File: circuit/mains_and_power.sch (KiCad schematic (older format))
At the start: 28 parts, among them J1 Screw_Terminal_01x10, U1 AQH3223, U2 AQH3223, U3 AQH3223, U4 MPM-05-12, U5 TC7660SEOA, U6 AP5100

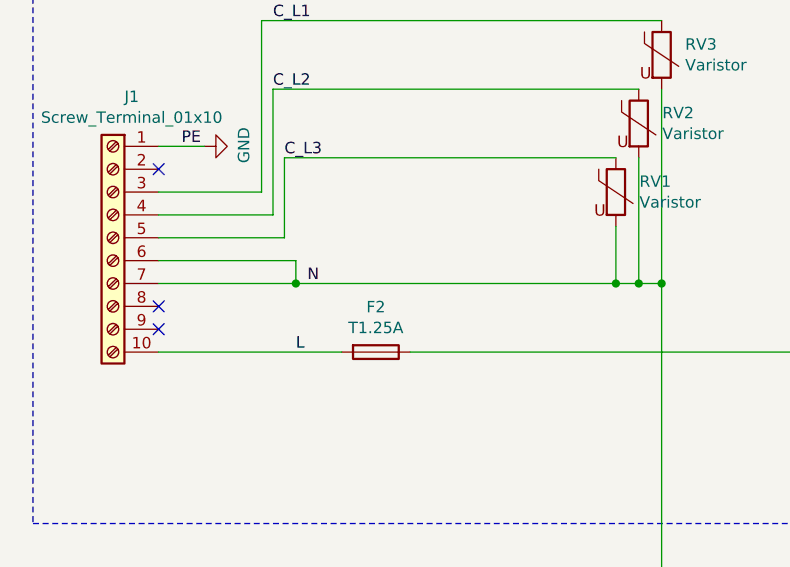
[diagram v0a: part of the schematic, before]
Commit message: Finish schematic rev1 and footprint assignment
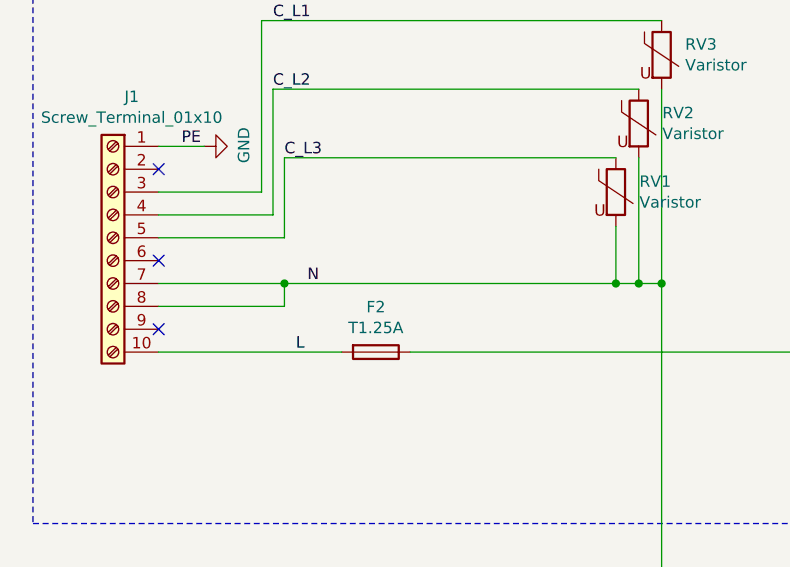
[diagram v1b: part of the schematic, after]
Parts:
- C1, C10, C11, C2, C3, C5, C6, C8: PartNo (none) -> 963-EMK212ABJ106MG-T
- C26: footprint (none) -> Capacitor_SMD:C_0805_2012Metric_Pad1.15x1.40mm_HandSolder; PartNo (none) -> 77-VJ0805Y101KXACBC
- C4, C7, C9: footprint Capacitor_SMD:C_0603_1608Metric_Pad1.05x0.95mm_HandSolder -> Capacitor_SMD:C_0805_2012Metric_Pad1.15x1.40mm_HandSolder; PartNo (none) -> 963-EMF212B7104KGHT
- J1: footprint (none) -> atmevse-footprints:CUI_TB005-762-10GR; PartNo 651-1707111 -> 490-TB005-762-10BE
- U1, U2, U3: PartNo (none) -> 769-AQH1213AX
- U4: footprint Converter_ACDC:Converter_ACDC_MeanWell_IRM-05-xx_THT -> Converter_ACDC:Converter_ACDC_MeanWell_IRM-10-xx_THT; PartNo (none) -> 709-IRM10-12
- U5: PartNo (none) -> 579-TC7660SEOA
- U6: PartNo (none) -> 621-AP5100WG-7
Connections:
- net N: now also J1.8 (Pin_8); no longer J1.6 (Pin_6)
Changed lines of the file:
@@
 Sheet 2 4
 Title ""
-Date "2020-05-29"
-Rev "0.7"
+Date "2020-06-01"
+Rev "1.0"
 Comp ""
 Comment1 "DONE: Replaced buck regulator AOZ1280 -> AP5100"
@@
 F 3 "" H 5200 3800 50  0001 C CNN
 F 4 "" H 5200 3800 50  0001 C CNN "Part"
-F 5 "" H 5200 3800 50  0001 C CNN "PartNo"
+F 5 "769-AQH1213AX" H 5200 3800 50  0001 C CNN "PartNo"
 F 6 "Mouser" H 5200 3800 50  0001 C CNN "Supplier"
 	1    5200 3800
@@
 F 3 "" H 5200 2800 50  0001 C CNN
 F 4 "" H 5200 2800 50  0001 C CNN "Part"
-F 5 "" H 5200 2800 50  0001 C CNN "PartNo"
+F 5 "769-AQH1213AX" H 5200 2800 50  0001 C CNN "PartNo"
 F 6 "Mouser" H 5200 2800 50  0001 C CNN "Supplier"
 	1    5200 2800
@@
 F 3 "" H 5200 1800 50  0001 C CNN
 F 4 "" H 5200 1800 50  0001 C CNN "Part"
-F 5 "" H 5200 1800 50  0001 C CNN "PartNo"
+F 5 "769-AQH1213AX" H 5200 1800 50  0001 C CNN "PartNo"
 F 6 "Mouser" H 5200 1800 50  0001 C CNN "Supplier"
 	1    5200 1800
@@
 F 0 "U4" H 5200 5447 42  0000 C CNN
 F 1 "MPM-05-12" H 5200 5368 42  0000 C CNN
-F 2 "Converter_ACDC:Converter_ACDC_MeanWell_IRM-05-xx_THT" H 5200 5000 50  0001 C CNN
+F 2 "Converter_ACDC:Converter_ACDC_MeanWell_IRM-10-xx_THT" H 5200 5000 50  0001 C CNN
 F 3 "https://www.meanwell.com/webapp/product/search.aspx?prod=MPM-05" H 5200 5000 50  0001 C CNN
 F 4 "" H 5200 5000 50  0001 C CNN "Part"
-F 5 "" H 5200 5000 50  0001 C CNN "PartNo"
+F 5 "709-IRM10-12" H 5200 5000 50  0001 C CNN "PartNo"
 F 6 "Mouser" H 5200 5000 50  0001 C CNN "Supplier"
 	1    5200 5000
@@
 F 3 "~" H 6700 1850 50  0001 C CNN
 F 4 "" H 6700 1850 50  0001 C CNN "Part"
-F 5 "" H 6700 1850 50  0001 C CNN "PartNo"
+F 5 "963-EMK212ABJ106MG-T" H 6700 1850 50  0001 C CNN "PartNo"
 F 6 "Mouser" H 6700 1850 50  0001 C CNN "Supplier"
 	1    6700 1850
@@
 F 3 "~" H 7050 1850 50  0001 C CNN
 F 4 "" H 7050 1850 50  0001 C CNN "Part"
-F 5 "" H 7050 1850 50  0001 C CNN "PartNo"
+F 5 "963-EMK212ABJ106MG-T" H 7050 1850 50  0001 C CNN "PartNo"
 F 6 "Mouser" H 7050 1850 50  0001 C CNN "Supplier"
 	1    7050 1850
@@
 F 3 "~" H 7400 1850 50  0001 C CNN
 F 4 "" H 7400 1850 50  0001 C CNN "Part"
-F 5 "" H 7400 1850 50  0001 C CNN "PartNo"
+F 5 "963-EMK212ABJ106MG-T" H 7400 1850 50  0001 C CNN "PartNo"
 F 6 "Mouser" H 7400 1850 50  0001 C CNN "Supplier"
 	1    7400 1850
@@
 F 3 "~" H 7750 1850 50  0001 C CNN
 F 4 "" H 7750 1850 50  0001 C CNN "Part"
-F 5 "" H 7750 1850 50  0001 C CNN "PartNo"
+F 5 "963-EMK212ABJ106MG-T" H 7750 1850 50  0001 C CNN "PartNo"
 F 6 "Mouser" H 7750 1850 50  0001 C CNN "Supplier"
 	1    7750 1850
@@
 F 0 "C7" H 8215 1896 50  0000 L CNN
 F 1 "100n" V 8250 1650 50  0000 L CNN
-F 2 "Capacitor_SMD:C_0603_1608Metric_Pad1.05x0.95mm_HandSolder" H 8138 1700 50  0001 C CNN
+F 2 "Capacitor_SMD:C_0805_2012Metric_Pad1.15x1.40mm_HandSolder" H 8138 1700 50  0001 C CNN
 F 3 "~" H 8100 1850 50  0001 C CNN
 F 4 "" H 8100 1850 50  0001 C CNN "Part"
-F 5 "" H 8100 1850 50  0001 C CNN "PartNo"
+F 5 "963-EMF212B7104KGHT " H 8100 1850 50  0001 C CNN "PartNo"
 F 6 "Mouser" H 8100 1850 50  0001 C CNN "Supplier"
 	1    8100 1850
@@
 F 0 "C9" V 9271 1550 50  0000 C CNN
 F 1 "100n" V 9362 1550 50  0000 C CNN
-F 2 "Capacitor_SMD:C_0603_1608Metric_Pad1.05x0.95mm_HandSolder" H 9500 1550 50  0001 C CNN
+F 2 "Capacitor_SMD:C_0805_2012Metric_Pad1.15x1.40mm_HandSolder" H 9500 1550 50  0001 C CNN
 F 3 "~" H 9500 1550 50  0001 C CNN
 F 4 "" H 9500 1550 50  0001 C CNN "Part"
-F 5 "" H 9500 1550 50  0001 C CNN "PartNo"
+F 5 "963-EMF212B7104KGHT " H 9500 1550 50  0001 C CNN "PartNo"
 F 6 "Mouser" H 9500 1550 50  0001 C CNN "Supplier"
 	1    9500 1550
@@
 F 3 "~" H 10700 1850 50  0001 C CNN
 F 4 "" H 10700 1850 50  0001 C CNN "Part"
-F 5 "" H 10700 1850 50  0001 C CNN "PartNo"
+F 5 "963-EMK212ABJ106MG-T" H 10700 1850 50  0001 C CNN "PartNo"
 F 6 "Mouser" H 10700 1850 50  0001 C CNN "Supplier"
 	1    10700 1850
@@
 F 3 "~" H 11000 1850 50  0001 C CNN
 F 4 "" H 11000 1850 50  0001 C CNN "Part"
-F 5 "" H 11000 1850 50  0001 C CNN "PartNo"
+F 5 "963-EMK212ABJ106MG-T" H 11000 1850 50  0001 C CNN "PartNo"
 F 6 "Mouser" H 11000 1850 50  0001 C CNN "Supplier"
 	1    11000 1850
@@
 F 3 "https://www.mouser.de/datasheet/2/268/21467B-1180369.pdf" H 8900 4350 50  0001 C CNN
 F 4 "" H 8900 4350 50  0001 C CNN "Part"
-F 5 "" H 8900 4350 50  0001 C CNN "PartNo"
+F 5 "579-TC7660SEOA" H 8900 4350 50  0001 C CNN "PartNo"
 F 6 "Mouser" H 8900 4350 50  0001 C CNN "Supplier"
 	1    8900 4350
@@
 F 0 "C4" H 7965 3996 50  0000 L CNN
 F 1 "100n" V 8000 3750 50  0000 L CNN
-F 2 "Capacitor_SMD:C_0603_1608Metric_Pad1.05x0.95mm_HandSolder" H 7888 3800 50  0001 C CNN
+F 2 "Capacitor_SMD:C_0805_2012Metric_Pad1.15x1.40mm_HandSolder" H 7888 3800 50  0001 C CNN
 F 3 "~" H 7850 3950 50  0001 C CNN
 F 4 "" H 7850 3950 50  0001 C CNN "Part"
-F 5 "" H 7850 3950 50  0001 C CNN "PartNo"
+F 5 "963-EMF212B7104KGHT " H 7850 3950 50  0001 C CNN "PartNo"
 F 6 "Mouser" H 7850 3950 50  0001 C CNN "Supplier"
 	1    7850 3950
@@
 F 3 "~" H 7500 4400 50  0001 C CNN
 F 4 "" H 7500 4400 50  0001 C CNN "Part"
-F 5 "" H 7500 4400 50  0001 C CNN "PartNo"
+F 5 "963-EMK212ABJ106MG-T" H 7500 4400 50  0001 C CNN "PartNo"
 F 6 "Mouser" H 7500 4400 50  0001 C CNN "Supplier"
 	1    7500 4400
@@
 F 3 "~" H 9700 4750 50  0001 C CNN
 F 4 "" H 9700 4750 50  0001 C CNN "Part"
-F 5 "" H 9700 4750 50  0001 C CNN "PartNo"
+F 5 "963-EMK212ABJ106MG-T" H 9700 4750 50  0001 C CNN "PartNo"
 F 6 "Mouser" H 9700 4750 50  0001 C CNN "Supplier"
 	1    9700 4750
@@
 F 0 "J1" H 818 3467 50  0000 C CNN
 F 1 "Screw_Terminal_01x10" H 818 3376 50  0000 C CNN
-F 2 "" H 900 2850 50  0001 C CNN
+F 2 "atmevse-footprints:CUI_TB005-762-10GR" H 900 2850 50  0001 C CNN
 F 3 "https://www.phoenixcontact.com/online/portal/us?uri=pxc-oc-itemdetail:pid=1707111&library=usen&pdfmode=direct&pdflanguage=en" H 900 2850 50  0001 C CNN
 F 4 "" H 900 2850 50  0001 C CNN "Part"
 F 5 "Mouser" H 900 2850 50  0001 C CNN "Supplier"
-F 6 "651-1707111 " H 900 2850 50  0001 C CNN "PartNo"
+F 6 "490-TB005-762-10BE" H 900 2850 50  0001 C CNN "PartNo"
 	1    900  2850
 	-1   0    0    -1
@@
 Text Label 1650 2500 0    50   ~ 0
 C_L3
-Wire Wire Line
-	1100 2950 1700 2950
 Text Label 1750 3050 0    50   ~ 0
 N
 Wire Wire Line
 	3300 2200 3300 3050
-Wire Wire Line
-	1100 3050 1700 3050
 Connection ~ 3300 3050
 Wire Wire Line
@@
 Wire Wire Line
 	3100 3050 3200 3050
-Wire Wire Line
-	1700 2950 1700 3050
-Connection ~ 1700 3050
-Wire Wire Line
-	1700 3050 3100 3050
 $Comp
 L power:GND #PWR01
@@
 Text Label 1700 3350 0    50   ~ 0
 L
-NoConn ~ 1100 3150
 NoConn ~ 1100 3250
 $Comp
@@
 F 3 "https://www.mouser.de/datasheet/2/115/AP5100-82364.pdf" H 8650 1400 50  0001 C CNN
 F 4 "Mouser" H 8900 1650 50  0001 C CNN "Supplier"
+F 5 "621-AP5100WG-7" H 8900 1650 50  0001 C CNN "PartNo"
 	1    8900 1650
 	1    0    0    -1
@@
 F 0 "C26" H 10442 1746 50  0000 L CNN
 F 1 "100p" V 10450 1500 50  0000 L CNN
-F 2 "" H 10350 1700 50  0001 C CNN
+F 2 "Capacitor_SMD:C_0805_2012Metric_Pad1.15x1.40mm_HandSolder" H 10350 1700 50  0001 C CNN
 F 3 "~" H 10350 1700 50  0001 C CNN
 F 4 "Mouser" H 10350 1700 50  0001 C CNN "Supplier"
+F 5 "77-VJ0805Y101KXACBC " H 10350 1700 50  0001 C CNN "PartNo"
 	1    10350 1700
 	1    0    0    -1
@@
 Wire Wire Line
 	10350 1850 10150 1850
+Wire Wire Line
+	1100 3050 1650 3050
+Wire Wire Line
+	1100 3150 1650 3150
+Wire Wire Line
+	1650 3150 1650 3050
+Connection ~ 1650 3050
+Wire Wire Line
+	1650 3050 3100 3050
+NoConn ~ 1100 2950
 $EndSCHEMATC

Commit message: Update doc
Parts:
- removed J1: Screw_Terminal_01x10, atmevse-footprints:CUI_TB005-762-10GR, symbol smartevse:Screw_Terminal_01x10
- added J? (x2): Screw_Terminal_01x05, symbol Connector:Screw_Terminal_01x05
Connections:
- net C_L1: now also J?.3 (Pin_3)
- net C_L2: now also J?.5 (Pin_5)
- net C_L3: now also J?.2 (Pin_2)
- net GND: now also J?.1 (Pin_1)
- net L: now also J?.5 (Pin_5)
- net N: now also J?.1 (Pin_1), J?.2 (Pin_2), J?.3 (Pin_3), J?.4 (Pin_4)
- no-connect marks 8 -> 6
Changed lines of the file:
@@
 $Descr A4 11693 8268
 encoding utf-8
-Sheet 2 4
-Title ""
-Date "2020-06-01"
-Rev "1.0"
+Sheet 2 5
+Title "FGCCS-Ctrl22"
+Date "2020-08-11"
+Rev "1.1"
 Comp ""
-Comment1 "DONE: Replaced buck regulator AOZ1280 -> AP5100"
-Comment2 "DONE: Edit SSR connections"
-Comment3 "TODO: verify CT input circuit in sim (maybe rectify signal?)"
-Comment4 "DONE: add bias voltage (VDD/2)"
+Comment1 ""
+Comment2 ""
+Comment3 ""
+Comment4 ""
 $EndDescr
 $Comp
@@
 Text Notes 9000 5400 2    50   ~ 0
 12V Inverter\n
-$Comp
-L smartevse:Screw_Terminal_01x10 J1
-U 1 1 5E9A97C9
-P 900 2850
-F 0 "J1" H 818 3467 50  0000 C CNN
-F 1 "Screw_Terminal_01x10" H 818 3376 50  0000 C CNN
-F 2 "atmevse-footprints:CUI_TB005-762-10GR" H 900 2850 50  0001 C CNN
-F 3 "https://www.phoenixcontact.com/online/portal/us?uri=pxc-oc-itemdetail:pid=1707111&library=usen&pdfmode=direct&pdflanguage=en" H 900 2850 50  0001 C CNN
-F 4 "" H 900 2850 50  0001 C CNN "Part"
-F 5 "Mouser" H 900 2850 50  0001 C CNN "Supplier"
-F 6 "490-TB005-762-10BE" H 900 2850 50  0001 C CNN "PartNo"
-	1    900  2850
-	-1   0    0    -1
-$EndComp
-NoConn ~ 1100 2550
 Wire Notes Line
 	550  750  550  4100
@@
 SSR_L3
 Wire Wire Line
-	1100 2650 1550 2650
-Wire Wire Line
-	1550 2650 1550 1900
-Wire Wire Line
 	1550 1900 3300 1900
 Text Label 1200 2450 0    50   ~ 0
@@
 C_L1
 Wire Wire Line
-	1600 2200 1600 2750
-Wire Wire Line
-	1600 2750 1100 2750
-Wire Wire Line
 	1600 2200 3200 2200
 Text Label 1600 2200 0    50   ~ 0
 C_L2
 Wire Wire Line
-	1100 2850 1650 2850
-Wire Wire Line
-	1650 2850 1650 2500
-Wire Wire Line
 	1650 2500 3100 2500
 Text Label 1650 2500 0    50   ~ 0
 C_L3
-Text Label 1750 3050 0    50   ~ 0
+Text Label 1750 3150 0    50   ~ 0
 N
 Wire Wire Line
@@
 Connection ~ 3300 3050
 Wire Wire Line
-	3300 3050 3300 5200
+	3300 3050 3300 3150
 Wire Wire Line
 	3200 2500 3200 3050
@@
 Wire Wire Line
 	3100 2800 3100 3050
-Connection ~ 3100 3050
 Wire Wire Line
 	3100 3050 3200 3050
@@
 Text Label 1700 3350 0    50   ~ 0
 L
-NoConn ~ 1100 3250
 $Comp
 L smartevse:FuseT1.25 F2
 U 1 1 5ECD985B
 P 2050 3350
-F 0 "F2" V 1853 3350 50  0000 C CNN
+F 0 "F2" V 2150 3350 50  0000 C CNN
 F 1 "T1.25A" V 1944 3350 50  0000 C CNN
 F 2 "smartevse-footprints:TE5" V 1980 3350 50  0001 C CNN
@@
 	10350 1850 10150 1850
 Wire Wire Line
-	1100 3050 1650 3050
-Wire Wire Line
-	1100 3150 1650 3150
-Wire Wire Line
-	1650 3150 1650 3050
-Connection ~ 1650 3050
-Wire Wire Line
-	1650 3050 3100 3050
-NoConn ~ 1100 2950
+	1100 3150 1300 3150
+$Comp
+L Connector:Screw_Terminal_01x05 J?
+U 1 1 5F37F01F
+P 900 2650
+F 0 "J?" H 818 3067 50  0000 C CNN
+F 1 "Screw_Terminal_01x05" H 818 2976 50  0000 C CNN
+F 2 "" H 900 2650 50  0001 C CNN
+F 3 "~" H 900 2650 50  0001 C CNN
+	1    900  2650
+	-1   0    0    -1
+$EndComp
+$Comp
+L Connector:Screw_Terminal_01x05 J?
+U 1 1 5F3809ED
+P 900 3150
+F 0 "J?" H 900 2850 50  0000 C CNN
+F 1 "Screw_Terminal_01x05" H 850 2750 50  0000 C CNN
+F 2 "" H 900 3150 50  0001 C CNN
+F 3 "~" H 900 3150 50  0001 C CNN
+	1    900  3150
+	-1   0    0    -1
+$EndComp
+NoConn ~ 1100 3250
+Wire Wire Line
+	1300 2550 1100 2550
+Wire Wire Line
+	1100 2750 1300 2750
+Connection ~ 1300 2750
+Wire Wire Line
+	1300 2750 1300 2550
+Wire Wire Line
+	1100 2950 1300 2950
+Connection ~ 1300 2950
+Wire Wire Line
+	1300 2950 1300 2750
+Wire Wire Line
+	1300 2950 1300 3150
+Connection ~ 1300 3150
+Wire Wire Line
+	1300 3150 3300 3150
+Connection ~ 3300 3150
+Wire Wire Line
+	3300 3150 3300 5200
+Wire Wire Line
+	1550 1900 1550 2650
+Wire Wire Line
+	1550 2650 1100 2650
+Wire Wire Line
+	1600 2200 1600 2850
+Wire Wire Line
+	1600 2850 1100 2850
+Wire Wire Line
+	1650 2500 1650 3050
+Wire Wire Line
+	1650 3050 1100 3050
 $EndSCHEMATC

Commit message: Testing build
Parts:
- gave numbers to parts that had none: 2
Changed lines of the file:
@@
 $Descr A4 11693 8268
 encoding utf-8
-Sheet 2 5
+Sheet 2 4
 Title "FGCCS-Ctrl22"
 Date "2020-08-11"
@@
 	1100 3150 1300 3150
 $Comp
-L Connector:Screw_Terminal_01x05 J?
+L Connector:Screw_Terminal_01x05 J1
 U 1 1 5F37F01F
 P 900 2650
-F 0 "J?" H 818 3067 50  0000 C CNN
+F 0 "J1" H 818 3067 50  0000 C CNN
 F 1 "Screw_Terminal_01x05" H 818 2976 50  0000 C CNN
 F 2 "" H 900 2650 50  0001 C CNN
@@
 $EndComp
 $Comp
-L Connector:Screw_Terminal_01x05 J?
+L Connector:Screw_Terminal_01x05 J2
 U 1 1 5F3809ED
 P 900 3150
-F 0 "J?" H 900 2850 50  0000 C CNN
+F 0 "J2" H 900 2850 50  0000 C CNN
 F 1 "Screw_Terminal_01x05" H 850 2750 50  0000 C CNN
 F 2 "" H 900 3150 50  0001 C CNN
